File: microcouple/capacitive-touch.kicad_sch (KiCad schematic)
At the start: 6 parts, among them J4 Conn_02x03_Odd_Even, U6 CAP1188

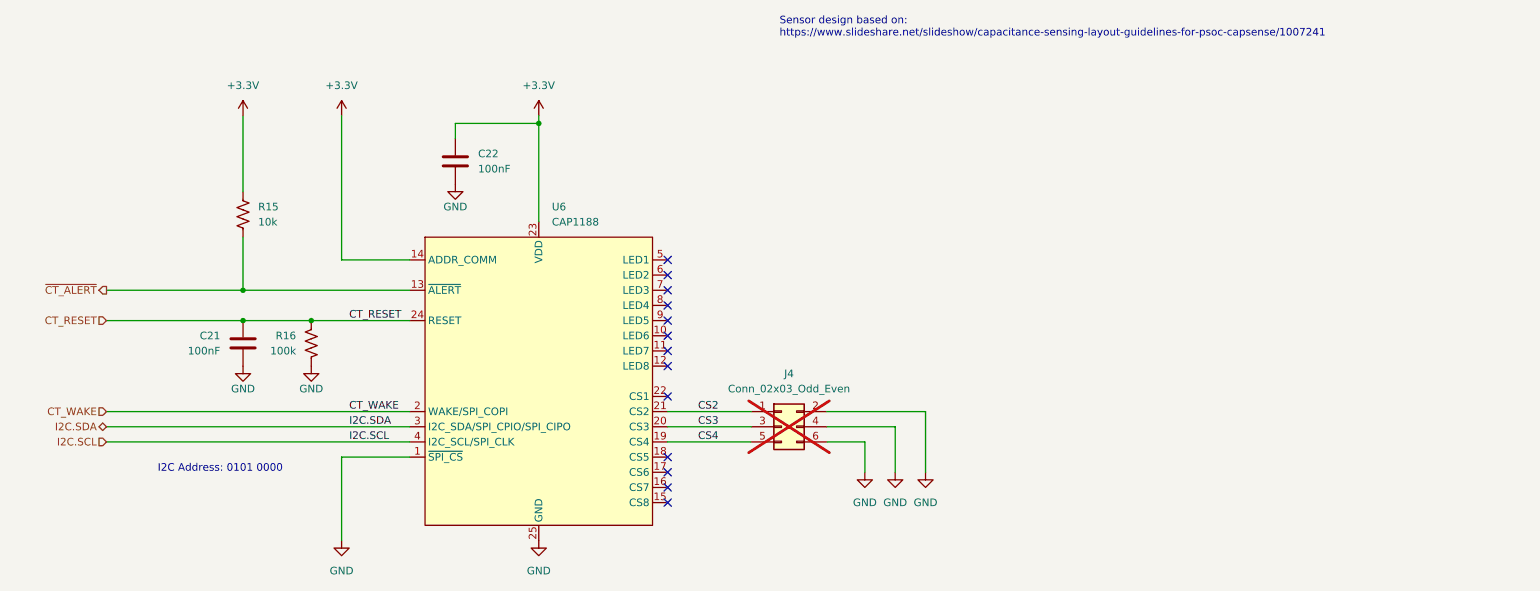
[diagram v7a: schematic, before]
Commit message: Update for JLCPCB
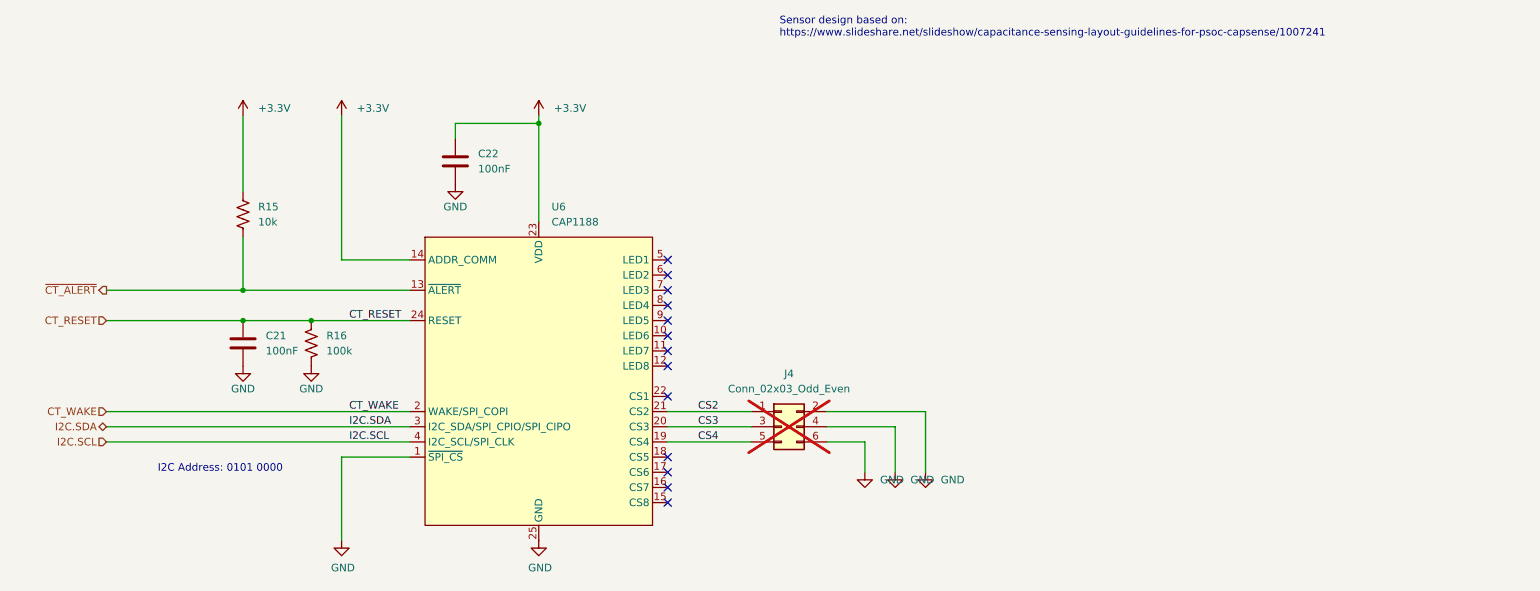
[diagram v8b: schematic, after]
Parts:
- C21, C22: footprint GS_SMD:0201_0603Metric -> GS_Capacitors:C_0201_0603Metric; symbol Device:C -> GS_Capacitor_0201:C_0201_100nF; LCSC ID (none) -> C18164587; Manufacturer (none) -> CCTC; Mfr. Part # (none) -> TCC0201X5R104M250ZT; Package (none) -> 0201
- R15: footprint GS_SMD:0201_0603Metric -> GS_Resistors:R_0201_0603Metric; symbol Device:R_US -> GS_Resistor_0201:R_0201_10k; LCSC ID (none) -> C304504; Manufacturer (none) -> FH (Guangdong Fenghua Advanced Tech); Mfr. Part # (none) -> RC-01W103JT; Package (none) -> 0201
- R16: footprint GS_SMD:0201_0603Metric -> GS_Resistors:R_0201_0603Metric; symbol Device:R_US -> GS_Resistor_0201:R_0201_100k; LCSC ID (none) -> C106224; Manufacturer (none) -> YAGEO; Mfr. Part # (none) -> RC0201FR-07100KL; Package (none) -> 0201
- U6: LCSC ID (none) -> C2652057; Manufacturer (none) -> Microchip Tech; Mfr. Part # (none) -> CAP1188-1-CP-TR; Package (none) -> QFN-24-EP(4x4)
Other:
- title: (none) -> Capacitive Touch
